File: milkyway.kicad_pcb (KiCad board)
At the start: 2 copper layers, 314.4 x 98.8 mm, 82 parts, among them J10 Conn_01x01, J11 Conn_01x01, J12 Conn_01x01, J13 Conn_01x01, J14 Conn_01x01, J15 Conn_01x01, J16 Conn_01x01, J17 Conn_01x01, J2 Conn_01x01, J3 Conn_01x01, J4 Conn_01x01, J5 Conn_01x01, J6 Conn_01x01, J7 Conn_01x01, J8 Conn_01x01, J9 Conn_01x01, SW1 SW_PUSH, SW10 SW_PUSH, SW11 SW_PUSH, SW12 SW_PUSH, SW13 SW_PUSH, SW14 SW_PUSH, SW15 SW_PUSH, SW16 SW_PUSH, SW17 KEY_SWITCH, SW17 SW_PUSH, SW18 SW_PUSH, SW19 SW_PUSH, SW2 KEY_SWITCH, SW2 SW_PUSH, SW22 SW_PUSH, SW23 SW_PUSH, SW24 SW_PUSH, SW27 SW_PUSH, SW28 SW_PUSH, SW29 SW_PUSH, SW3 SW_PUSH, SW32 SW_PUSH, SW33 SW_PUSH, SW34 SW_PUSH, SW37 SW_PUSH, SW38 SW_PUSH, SW39 SW_PUSH, SW4 KEY_SWITCH, SW4 SW_PUSH, SW42 SW_PUSH, SW43 SW_PUSH, SW44 SW_PUSH, SW47 SW_PUSH, SW48 SW_PUSH, SW49 SW_PUSH, SW5 SW_PUSH, SW52 SW_PUSH, SW53 SW_PUSH, SW54 SW_PUSH, SW57 SW_PUSH, SW58 SW_PUSH, SW6 SW_PUSH, SW60 SW_PUSH, SW61 SW_PUSH, SW62 SW_PUSH, SW67 SW_PUSH, SW7 SW_PUSH, SW72 SW_PUSH, SW8 SW_PUSH, SW9 SW_PUSH

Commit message: complete plate
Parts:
- removed SW15, SW16, SW72: SW_PUSH, kbd_SW_Hole:SW_Hole_1u
- removed the SW2 at (171.4, 104.8)
- removed the SW2 at (261.9, 104.8)
- removed the SW2 at (309.6, 104.8)
- removed the SW2 at (33.3, 104.8)
- removed the SW2 at (81.0, 104.8)
- removed SW62: SW_PUSH, kbd_SW_Hole:SW_Hole_1.75u
- removed the SW9 at (57.1, 104.8)
- removed the SW9 at (285.8, 104.8)
- added SW2: KEY_SWITCH, milkyway:SW_Hole_Split_Bksp, F.Cu at (304.8, 28.6)
- added SW2: KEY_SWITCH, milkyway:SW_Hole_Split_Rshift, F.Cu at (297.7, 85.7)
- added SW2: KEY_SWITCH, milkyway:SW_Hole_R5_all, F.Cu at (171.4, 104.8)
- turned SW4 to 0 degrees (x2)

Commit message: complete pcb
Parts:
- removed J2, J3, J4, J5, J6, J7: Conn_01x01, kbd_Hole:m2_Screw_Hole_EdgeCuts
- removed SW1, SW10, SW11, SW12 (x2), SW13 (x2), SW14 (x2), SW17, SW18 (x2), SW19, SW2, SW22, SW23, SW24, SW27, SW28, SW29, SW3, SW32, SW33, SW34, SW37, SW38, SW39, SW4, SW42, SW43, SW44, SW47, SW48, SW49, SW5, SW52, SW53, SW54, SW57, SW58, SW6, SW60 (x2), SW61, SW67, SW7, SW8 (x2), SW9 (x2): SW_PUSH, kbd_SW_Hole:SW_Hole_1u
- removed SW17, SW2: KEY_SWITCH, kbd_SW_Hole:SW_Hole_1.5u
- removed SW2: KEY_SWITCH, milkyway:SW_Hole_Split_Bksp
- removed SW2: KEY_SWITCH, milkyway:SW_Hole_Split_Rshift
- removed SW2: KEY_SWITCH, milkyway:SW_Hole_R5_all
- removed SW3: SW_PUSH, kbd_SW_Hole:SW_Hole_1.75u
- removed SW4 (x2): KEY_SWITCH, kbd_SW_Hole:SW_Hole_2.25u
- added DC00: D, kbd_Parts:Diode_TH_SMD, F.Cu at (57.1, 33.3)
- added DC01: D, kbd_Parts:Diode_TH_SMD, F.Cu at (95.2, 33.3)
- added DC02: D, kbd_Parts:Diode_TH_SMD, F.Cu at (133.3, 33.3)
- added DC03: D, kbd_Parts:Diode_TH_SMD, F.Cu at (171.4, 33.3)
- added DC04: D, kbd_Parts:Diode_TH_SMD, F.Cu at (209.6, 33.3)
- added DC05: D, kbd_Parts:Diode_TH_SMD, F.Cu at (246.4, 30.5)
- added DC06: D, kbd_Parts:Diode_TH_SMD, F.Cu at (284.5, 31.1)
- added DC07: D, kbd_Parts:Diode_TH_SMD, F.Cu at (321.5, 42.9)
- added DC10: D, kbd_Parts:Diode_TH_SMD, F.Cu at (66.7, 52.4)
- added DC11: D, kbd_Parts:Diode_TH_SMD, F.Cu at (104.8, 52.4)
- added DC12: D, kbd_Parts:Diode_TH_SMD, F.Cu at (142.9, 52.4)
- added DC13: D, kbd_Parts:Diode_TH_SMD, F.Cu at (181.0, 52.4)
- added DC14: D, kbd_Parts:Diode_TH_SMD, F.Cu at (219.1, 52.4)
- added DC15: D, kbd_Parts:Diode_TH_SMD, F.Cu at (257.2, 52.4)
- added DC16: D, kbd_Parts:Diode_TH_SMD, F.Cu at (295.3, 52.4)
- added DC20: D, kbd_Parts:Diode_TH_SMD, F.Cu at (71.4, 71.4)
- added DC21: D, kbd_Parts:Diode_TH_SMD, F.Cu at (109.5, 71.4)
- added DC22: D, kbd_Parts:Diode_TH_SMD, F.Cu at (147.6, 71.4)
- added DC23: D, kbd_Parts:Diode_TH_SMD, F.Cu at (185.7, 71.4)
- added DC24: D, kbd_Parts:Diode_TH_SMD, F.Cu at (223.8, 71.4)
- added DC25: D, kbd_Parts:Diode_TH_SMD, F.Cu at (261.9, 71.4)
- added DC26: D, kbd_Parts:Diode_TH_SMD, F.Cu at (283.4, 71.4)
- added DC30: D, kbd_Parts:Diode_TH_SMD, F.Cu at (81.0, 90.5)
- added DC31: D, kbd_Parts:Diode_TH_SMD, F.Cu at (118.1, 90.5)
- added DC32: D, kbd_Parts:Diode_TH_SMD, F.Cu at (157.2, 90.5)
- added DC33: D, kbd_Parts:Diode_TH_SMD, F.Cu at (194.3, 88.4)
- added DC34: D, kbd_Parts:Diode_TH_SMD, F.Cu at (233.4, 90.5)
- added DC35: D, kbd_Parts:Diode_TH_SMD, F.Cu at (271.5, 90.5)
- added DC36: D, kbd_Parts:Diode_TH_SMD, F.Cu at (317.5, 95.2)
- added DC40: D, kbd_Parts:Diode_TH_SMD, F.Cu at (72.4, 109.6)
- added DC41: D, kbd_Parts:Diode_TH_SMD, F.Cu at (131.0, 95.2)
- added DC42: D, kbd_Parts:Diode_TH_SMD, F.Cu at (207.2, 100.0)
- added DC45: D, kbd_Parts:Diode_TH_SMD, F.Cu at (271.5, 109.5)
- added DC46: D, kbd_Parts:Diode_TH_SMD, F.Cu at (297.7, 109.5)
- added DR00: D, kbd_Parts:Diode_TH_SMD, F.Cu at (38.1, 33.3)
- added DR01: D, kbd_Parts:Diode_TH_SMD, F.Cu at (76.2, 33.3)
- added DR02: D, kbd_Parts:Diode_TH_SMD, F.Cu at (114.3, 33.3)
- added DR03: D, kbd_Parts:Diode_TH_SMD, F.Cu at (152.4, 33.3)
- added DR04: D, kbd_Parts:Diode_TH_SMD, F.Cu at (190.5, 32.7)
- added DR05: D, kbd_Parts:Diode_TH_SMD, F.Cu at (228.6, 33.3)
- added DR06: D, kbd_Parts:Diode_TH_SMD, F.Cu at (265.4, 31.1)
- added DR07: D, kbd_Parts:Diode_TH_SMD, F.Cu at (304.8, 38.1)
- added DR10: D, kbd_Parts:Diode_TH_SMD, F.Cu at (42.9, 52.4)
- added DR11: D, kbd_Parts:Diode_TH_SMD, F.Cu at (85.7, 52.4)
- added DR12: D, kbd_Parts:Diode_TH_SMD, F.Cu at (123.8, 52.4)
- added DR13: D, kbd_Parts:Diode_TH_SMD, F.Cu at (161.9, 52.4)
- added DR14: D, kbd_Parts:Diode_TH_SMD, F.Cu at (200.0, 52.4)
- added DR15: D, kbd_Parts:Diode_TH_SMD, F.Cu at (238.1, 52.4)
- added DR16: D, kbd_Parts:Diode_TH_SMD, F.Cu at (276.2, 52.4)
- added DR17: D, kbd_Parts:Diode_TH_SMD, F.Cu at (297.7, 52.4)
- added DR20: D, kbd_Parts:Diode_TH_SMD, F.Cu at (45.2, 71.4)
- added DR21: D, kbd_Parts:Diode_TH_SMD, F.Cu at (90.5, 71.4)
- added DR22: D, kbd_Parts:Diode_TH_SMD, F.Cu at (128.6, 71.4)
- added DR23: D, kbd_Parts:Diode_TH_SMD, F.Cu at (166.7, 71.4)
- added DR24: D, kbd_Parts:Diode_TH_SMD, F.Cu at (204.8, 71.4)
- added DR25: D, kbd_Parts:Diode_TH_SMD, F.Cu at (242.9, 71.4)
- added DR26: D, kbd_Parts:Diode_TH_SMD, F.Cu at (281.0, 71.4)
- added DR30: D, kbd_Parts:Diode_TH_SMD, F.Cu at (59.5, 90.5)
- added DR31: D, kbd_Parts:Diode_TH_SMD, F.Cu at (100.0, 90.5)
- added DR32: D, kbd_Parts:Diode_TH_SMD, F.Cu at (138.1, 90.5)
- added DR33: D, kbd_Parts:Diode_TH_SMD, F.Cu at (176.2, 90.5)
- added DR34: D, kbd_Parts:Diode_TH_SMD, F.Cu at (213.4, 88.3)
- added DR35: D, kbd_Parts:Diode_TH_SMD, F.Cu at (252.4, 90.5)
- added DR36: D, kbd_Parts:Diode_TH_SMD, F.Cu at (273.8, 90.5)
- added DR40: D, kbd_Parts:Diode_TH_SMD, F.Cu at (42.9, 109.5)
- added DR41: D, kbd_Parts:Diode_TH_SMD, F.Cu at (90.5, 95.2)
- added DR42: D, kbd_Parts:Diode_TH_SMD, F.Cu at (152.4, 109.5)
- added DR43: D, kbd_Parts:Diode_TH_SMD, F.Cu at (207.2, 109.5)
- added DR46: D, kbd_Parts:Diode_TH_SMD, F.Cu at (295.3, 109.5)
- added SW0: SW_PUSH, kbd_Parts:ResetSW, F.Cu at (219.1, 37.2)
- added SWC00: SW_PUSH, kbd_SW:CherryMX_Hotswap_1u, F.Cu at (47.6, 28.6)
- added SWC01: SW_PUSH, kbd_SW:CherryMX_Hotswap_1u, F.Cu at (85.7, 28.6)
- added SWC02: SW_PUSH, kbd_SW:CherryMX_Hotswap_1u, F.Cu at (123.8, 28.6)
- added SWC03: Enc, milkyway:CherryMX_Hotswap_1u_EC12, F.Cu at (161.9, 28.6)
- added SWC04: SW_PUSH, kbd_SW:CherryMX_Hotswap_1u, F.Cu at (200.0, 28.6)
- added SWC05: SW_PUSH, kbd_SW:CherryMX_Hotswap_1u, F.Cu at (238.1, 28.6)
- added SWC06: SW_PUSH, kbd_SW:CherryMX_Hotswap_1u, F.Cu at (276.2, 28.6)
- added SWC07: SW_PUSH, kbd_SW:CherryMX_Hotswap_1u, F.Cu at (314.3, 28.6)
- added SWC10: SW_PUSH, kbd_SW:CherryMX_Hotswap_1u, F.Cu at (57.1, 47.6)
- added SWC11: SW_PUSH, kbd_SW:CherryMX_Hotswap_1u, F.Cu at (95.2, 47.6)
- added SWC12: SW_PUSH, kbd_SW:CherryMX_Hotswap_1u, F.Cu at (133.3, 47.6)
- added SWC13: SW_PUSH, kbd_SW:CherryMX_Hotswap_1u, F.Cu at (171.4, 47.6)
- added SWC14: SW_PUSH, kbd_SW:CherryMX_Hotswap_1u, F.Cu at (209.6, 47.6)
- added SWC15: SW_PUSH, kbd_SW:CherryMX_Hotswap_1u, F.Cu at (247.7, 47.6)
- added SWC16: SW_PUSH, kbd_SW:CherryMX_Hotswap_1u, F.Cu at (285.8, 47.6)
- added SWC20: SW_PUSH, kbd_SW:CherryMX_Hotswap_1u, F.Cu at (61.9, 66.7)
- added SWC21: SW_PUSH, kbd_SW:CherryMX_Hotswap_1u, F.Cu at (100.0, 66.7)
- added SWC22: SW_PUSH, kbd_SW:CherryMX_Hotswap_1u, F.Cu at (138.1, 66.7)
- added SWC23: SW_PUSH, kbd_SW:CherryMX_Hotswap_1u, F.Cu at (176.2, 66.7)
- added SWC24: SW_PUSH, kbd_SW:CherryMX_Hotswap_1u, F.Cu at (214.3, 66.7)
- added SWC25: SW_PUSH, kbd_SW:CherryMX_Hotswap_1u, F.Cu at (252.4, 66.7)
- added SWC26: SW_PUSH, kbd_SW:CherryMX_Hotswap_2.25u, F.Cu at (302.4, 66.7)
- added SWC30: SW_PUSH, kbd_SW:CherryMX_Hotswap_1u, F.Cu at (71.4, 85.7)
- added SWC31: SW_PUSH, kbd_SW:CherryMX_Hotswap_1u, F.Cu at (109.5, 85.7)
- added SWC32: SW_PUSH, kbd_SW:CherryMX_Hotswap_1u, F.Cu at (147.6, 85.7)
- added SWC33: SW_PUSH, kbd_SW:CherryMX_Hotswap_1u, F.Cu at (185.7, 85.7)
- added SWC34: SW_PUSH, kbd_SW:CherryMX_Hotswap_1u, F.Cu at (223.8, 85.7)
- added SWC35: SW_PUSH, kbd_SW:CherryMX_Hotswap_1u, F.Cu at (261.9, 85.7)
- added SWC36: SW_PUSH, kbd_SW:CherryMX_Hotswap_1u, F.Cu at (314.3, 85.7)
- added SWC401: SW_PUSH, kbd_SW:CherryMX_Hotswap_1u, F.Cu at (57.1, 104.8)
- added SWC402: SW_PUSH, kbd_SW:CherryMX_Hotswap_1.5u, F.Cu at (61.9, 104.8)
- added SWC411: SW_PUSH, milkyway:CherryMX_Solder_3u_Rev, F.Cu at (123.8, 104.8)
- added SWC412: SW_PUSH, kbd_SW:CherryMX_1u_solder, F.Cu at (104.8, 104.8)
- added SWC421: Enc, milkyway:CherryMX_Solder_1u_EC12, F.Cu at (181.0, 104.8)
- added SWC422: SW_PUSH, milkyway:CherryMX_Solder_8u7u_Rev, F.Cu at (171.4, 104.8)
- added SWC423: SW_PUSH, milkyway:CherryMX_Solder_2.75u_Rev, F.Cu at (178.6, 104.8)
- added SWC451: SW_PUSH, kbd_SW:CherryMX_Hotswap_1.5u, F.Cu at (261.9, 104.8)
- added SWC452: SW_PUSH, kbd_SW:CherryMX_Hotswap_1.5u, F.Cu at (252.4, 104.8)
- added SWC46: SW_PUSH, kbd_SW:CherryMX_Hotswap_1.5u, F.Cu at (309.6, 104.8)
- added SWR00: SW_PUSH, kbd_SW:CherryMX_Hotswap_1u, F.Cu at (28.6, 28.6)
- added SWR01: SW_PUSH, kbd_SW:CherryMX_Hotswap_1u, F.Cu at (66.7, 28.6)
- added SWR02: SW_PUSH, kbd_SW:CherryMX_Hotswap_1u, F.Cu at (104.8, 28.6)
- added SWR03: Enc, milkyway:CherryMX_Hotswap_1u_EC12, F.Cu at (142.9, 28.6)
- added SWR04: SW_PUSH, kbd_SW:CherryMX_Hotswap_1u, F.Cu at (181.0, 28.6)
- added SWR05: SW_PUSH, kbd_SW:CherryMX_Hotswap_1u, F.Cu at (219.1, 28.6)
- added SWR06: SW_PUSH, kbd_SW:CherryMX_Hotswap_1u, F.Cu at (257.2, 28.6)
- added SWR071: SW_PUSH, kbd_SW:CherryMX_Hotswap_2u, F.Cu at (304.8, 28.6)
- added SWR072: SW_PUSH, kbd_SW:CherryMX_Hotswap_1u, F.Cu at (295.3, 28.6)
- added SWR10: SW_PUSH, kbd_SW:CherryMX_Hotswap_1.5u, F.Cu at (33.3, 47.6)
- added SWR11: SW_PUSH, kbd_SW:CherryMX_Hotswap_1u, F.Cu at (76.2, 47.6)
- added SWR12: SW_PUSH, kbd_SW:CherryMX_Hotswap_1u, F.Cu at (114.3, 47.6)
- added SWR13: Enc, milkyway:CherryMX_Hotswap_1u_EC12, F.Cu at (152.4, 47.6)
- added SWR14: SW_PUSH, kbd_SW:CherryMX_Hotswap_1u, F.Cu at (190.5, 47.6)
- added SWR15: SW_PUSH, kbd_SW:CherryMX_Hotswap_1u, F.Cu at (228.6, 47.6)
- added SWR16: SW_PUSH, kbd_SW:CherryMX_Hotswap_1u, F.Cu at (266.7, 47.6)
- added SWR17: SW_PUSH, kbd_SW:CherryMX_Hotswap_1.5u, F.Cu at (307.2, 47.6)
- added SWR201: SW_PUSH, kbd_SW:CherryMX_Hotswap_1.75u, F.Cu at (35.7, 66.7)
- added SWR202: SW_PUSH, kbd_SW:CherryMX_Hotswap_1u, F.Cu at (28.6, 66.7)
- added SWR21: SW_PUSH, kbd_SW:CherryMX_Hotswap_1u, F.Cu at (81.0, 66.7)
- added SWR22: SW_PUSH, kbd_SW:CherryMX_Hotswap_1u, F.Cu at (119.1, 66.7)
- added SWR23: Enc, milkyway:CherryMX_Hotswap_1u_EC12, F.Cu at (157.2, 66.7)
- added SWR24: SW_PUSH, kbd_SW:CherryMX_Hotswap_1u, F.Cu at (195.3, 66.7)
- added SWR25: SW_PUSH, kbd_SW:CherryMX_Hotswap_1u, F.Cu at (233.4, 66.7)
- added SWR26: SW_PUSH, kbd_SW:CherryMX_Hotswap_1u, F.Cu at (271.5, 66.7)
- added SWR30: SW_PUSH, kbd_SW:CherryMX_Hotswap_2.75u, F.Cu at (40.5, 85.7)
- added SWR31: SW_PUSH, kbd_SW:CherryMX_Hotswap_1u, F.Cu at (90.5, 85.7)
- added SWR32: SW_PUSH, kbd_SW:CherryMX_Hotswap_1u, F.Cu at (128.6, 85.7)
- added SWR33: Enc, milkyway:CherryMX_Hotswap_1u_EC12, F.Cu at (166.7, 85.7)
- added SWR34: SW_PUSH, kbd_SW:CherryMX_Hotswap_1u, F.Cu at (204.8, 85.7)
- added SWR35: SW_PUSH, kbd_SW:CherryMX_Hotswap_1u, F.Cu at (242.9, 85.7)
- added SWR361: SW_PUSH, kbd_SW:CherryMX_Hotswap_2.75u, F.Cu at (297.7, 85.7)
- added SWR362: SW_PUSH, kbd_SW:CherryMX_Hotswap_1.75u, F.Cu at (288.1, 85.7)
- added SWR40: SW_PUSH, kbd_SW:CherryMX_Hotswap_1.5u, F.Cu at (33.3, 104.8)
- added SWR411: SW_PUSH, kbd_SW:CherryMX_Hotswap_1.5u, F.Cu at (81.0, 104.8)
- added SWR412: SW_PUSH, kbd_SW:CherryMX_Hotswap_1.5u, F.Cu at (90.5, 104.8)
- added SWR421: Enc, milkyway:CherryMX_Solder_1u_EC12, F.Cu at (161.9, 104.8)
- added SWR422: SW_PUSH, milkyway:CherryMX_Solder_2u_Rev, F.Cu at (133.3, 104.8)
- added SWR431: SW_PUSH, milkyway:CherryMX_Solder_3u_Rev, F.Cu at (219.1, 104.8)
- added SWR432: SW_PUSH, milkyway:CherryMX_Solder_2.25u_Rev, F.Cu at (226.2, 104.8)
- added SWR461: SW_PUSH, kbd_SW:CherryMX_Hotswap_1u, F.Cu at (285.8, 104.8)
- added SWR462: SW_PUSH, kbd_SW:CherryMX_Hotswap_1.5u, F.Cu at (281.0, 104.8)
- added U1: Raspberry_Pi_Pico, milkyway:Raspberry_Pi_Pico, F.Cu at (261.9, 28.6)
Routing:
- net Col0: track 0.00 -> 505.5 mm, vias 0 -> 1
- net Col1: track 0.00 -> 443.4 mm, vias 0 -> 6
- net Row3: track 0.00 -> 435.4 mm, vias 0 -> 3
- net Col2: track 0.00 -> 429.7 mm, vias 0 -> 8
- net Row4: track 0.00 -> 417.8 mm, vias 0 -> 1
- net Row0: track 0.00 -> 404.9 mm
- net Row1: track 0.00 -> 379.8 mm
- net GND: track 0.00 -> 377.6 mm, vias 0 -> 4
- net Row2: track 0.00 -> 373.8 mm
- net Col3: track 0.00 -> 349.9 mm, vias 0 -> 8
- net Col6: track 0.00 -> 284.5 mm, vias 0 -> 6
- net Col5: track 0.00 -> 256.1 mm, vias 0 -> 6
- net Col4: track 0.00 -> 254.4 mm, vias 0 -> 5
- net Rot5B: track 0.00 -> 192.9 mm, vias 0 -> 4
- net Rot5A: track 0.00 -> 181.6 mm, vias 0 -> 4
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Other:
- board size 314.4 x 98.8 mm -> 304.4 x 98.8 mm

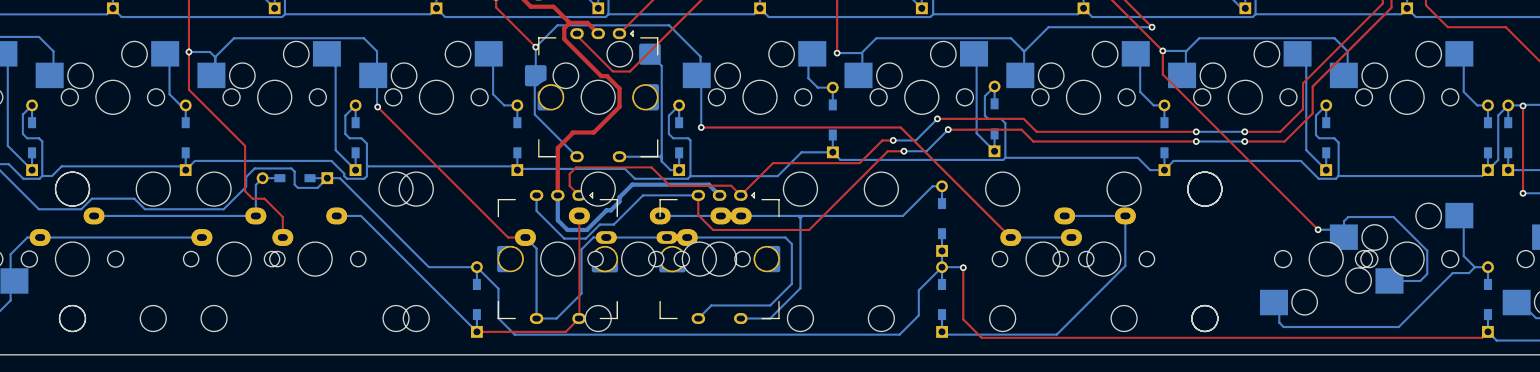
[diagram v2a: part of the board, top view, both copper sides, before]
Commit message: スタビバー上を通る配線を修正
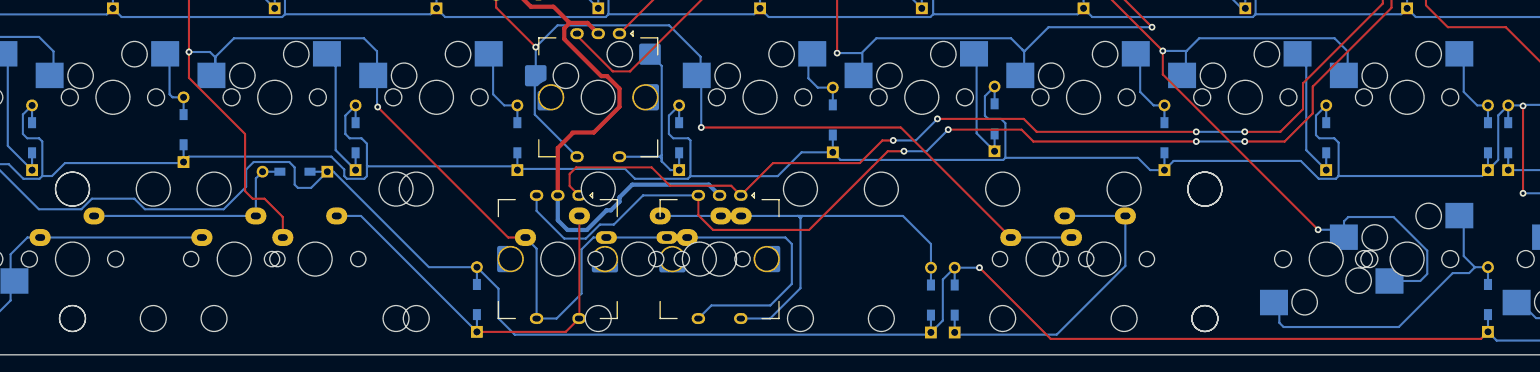
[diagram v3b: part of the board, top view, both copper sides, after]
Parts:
- moved DC42 9.68 mm to (205.9, 109.6)
- moved DR43 1.49 mm to (208.7, 109.6)
- moved DC31 0.99 mm to (117.9, 89.5)
- moved DC41 0.76 mm to (131.0, 94.5)
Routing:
- net Row4: track 417.8 -> 415.5 mm
- net Net-(DR43-Pad1): track 40.1 -> 38.6 mm
- net Net-(DC42-Pad2): track 54.8 -> 56.2 mm
- net Net-(DC41-Pad2): track 25.9 -> 26.6 mm
- net Net-(DC31-Pad2): track 9.65 -> 9.00 mm

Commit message: footprint miss thx salicylic acid san
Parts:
- SWR30: footprint kbd_SW:CherryMX_Hotswap_2.75u -> kbd_SW:CherryMX_Hotswap_2.25u
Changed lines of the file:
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@@
       (net 32 "Net-(DC34-Pad2)") (pinfunction "2") (pintype "passive"))
   )
-  (footprint "kbd_SW:CherryMX_Hotswap_2.75u" (layer "F.Cu")
+  (footprint "kbd_SW:CherryMX_Hotswap_2.25u" (layer "F.Cu")
     (at 40.48125 85.725)
     (property "Sheetfile" "milkyway.kicad_sch")
     (property "Sheetname" "")
     (attr smd)
-    (fp_text reference "SWR30" (at 7.402499 8.08) (layer "F.SilkS") hide
-      (effects (font (size 1 1) (thickness 0.15)))
+    (fp_text reference "SWR30" (at 0 4.7625) (layer "B.SilkS")
+      (effects (font (size 1 1) (thickness 0.15)) (justify mirror))
     )
     (fp_text value "SW_PUSH" (at -6.997501 -8.12) (layer "F.Fab") hide
       (effects (font (size 1 1) (thickness 0.15)))
     )
+    (fp_line (start -6.08 -0.876) (end -2.47 -0.876) (layer "B.SilkS") (width 0.15))
+    (fp_line (start 4.82 -2.876) (end 4.82 -6.784) (layer "B.SilkS") (width 0.15))
+    (fp_line (start 4.82 -6.784) (end -3.805 -6.784) (layer "B.SilkS") (width 0.15))
     (fp_line (start 4.82 -2.83) (end -0.23 -2.784) (layer "B.SilkS") (width 0.15))
-    (fp_line (start -6.08 -0.876) (end -2.47 -0.876) (layer "B.SilkS") (width 0.15))
-    (fp_line (start 4.82 -6.784) (end -3.805 -6.784) (layer "B.SilkS") (width 0.15))
-    (fp_line (start 4.82 -2.876) (end 4.82 -6.784) (layer "B.SilkS") (width 0.15))
     (fp_line (start -6.08 -4.83) (end -6.08 -0.885) (layer "B.SilkS") (width 0.15))
+    (fp_arc (start -2.465 -0.9) (mid -1.724361 -2.308061) (end -0.205 -2.78) (layer "B.SilkS") (width 0.15))
     (fp_arc (start -6.069 -4.9) (mid -5.327189 -6.31089) (end -3.805 -6.784) (layer "B.SilkS") (width 0.15))
-    (fp_arc (start -2.465 -0.9) (mid -1.724361 -2.308061) (end -0.205 -2.78) (layer "B.SilkS") (width 0.15))
     (fp_poly (pts
         (xy -6.08 -0.86)
@@
         (xy -6.09 -4.22)
       ) (layer "B.SilkS") (width 0.15) (fill solid))
-    (fp_line (start 26.19 -9.525) (end -26.19 -9.525) (layer "F.Fab") (width 0.15))
+    (fp_line (start 6 -7) (end 7 -7) (layer "F.Fab") (width 0.15))
+    (fp_line (start 21.43125 -9.525) (end -21.43125 -9.525) (layer "F.Fab") (width 0.15))
+    (fp_line (start -7 7) (end -7 6) (layer "F.Fab") (width 0.15))
+    (fp_line (start -7 -6) (end -7 -7) (layer "F.Fab") (width 0.15))
+    (fp_line (start 7 -7) (end 7 -6) (layer "F.Fab") (width 0.15))
+    (fp_line (start -21.43125 -9.525) (end -21.43125 9.525) (layer "F.Fab") (width 0.15))
+    (fp_line (start -7 -7) (end -6 -7) (layer "F.Fab") (width 0.15))
+    (fp_line (start 21.43125 9.525) (end 21.43125 -9.525) (layer "F.Fab") (width 0.15))
+    (fp_line (start -21.43125 9.525) (end 21.43125 9.525) (layer "F.Fab") (width 0.15))
+    (fp_line (start 7 6) (end 7 7) (layer "F.Fab") (width 0.15))
     (fp_line (start 7 7) (end 6 7) (layer "F.Fab") (width 0.15))
     (fp_line (start -6 7) (end -7 7) (layer "F.Fab") (width 0.15))
-    (fp_line (start 26.19 9.525) (end 26.19 -9.525) (layer "F.Fab") (width 0.15))
-    (fp_line (start -26.19 -9.525) (end -26.19 9.525) (layer "F.Fab") (width 0.15))
-    (fp_line (start 7 6) (end 7 7) (layer "F.Fab") (width 0.15))
-    (fp_line (start -7 -6) (end -7 -7) (layer "F.Fab") (width 0.15))
-    (fp_line (start 7 -7) (end 7 -6) (layer "F.Fab") (width 0.15))
-    (fp_line (start 6 -7) (end 7 -7) (layer "F.Fab") (width 0.15))
-    (fp_line (start -26.19 9.525) (end 26.19 9.525) (layer "F.Fab") (width 0.15))
-    (fp_line (start -7 -7) (end -6 -7) (layer "F.Fab") (width 0.15))
-    (fp_line (start -7 7) (end -7 6) (layer "F.Fab") (width 0.15))
     (pad "" np_thru_hole circle locked (at 11.9 -7 180) (size 3.05 3.05) (drill 3.05) (layers *.Cu *.Mask))
+    (pad "" np_thru_hole circle locked (at -3.81 -2.54 180) (size 3 3) (drill 3) (layers *.Cu *.Mask))
+    (pad "" np_thru_hole circle locked (at -5.08 0) (size 1.8 1.8) (drill 1.8) (layers *.Cu *.Mask))
     (pad "" np_thru_hole circle locked (at 5.08 0) (size 1.8 1.8) (drill 1.8) (layers *.Cu *.Mask))
     (pad "" np_thru_hole circle locked (at -11.9 -7 180) (size 3.05 3.05) (drill 3.05) (layers *.Cu *.Mask))
+    (pad "" np_thru_hole circle locked (at 11.9 8.24 180) (size 4 4) (drill 4) (layers *.Cu *.Mask))
     (pad "" np_thru_hole circle locked (at 0 0 90) (size 4 4) (drill 4) (layers *.Cu *.Mask))
-    (pad "" np_thru_hole circle locked (at 11.9 8.24 180) (size 4 4) (drill 4) (layers *.Cu *.Mask))
+    (pad "" np_thru_hole circle locked (at 2.54 -5.08 180) (size 3 3) (drill 3) (layers *.Cu *.Mask))
     (pad "" np_thru_hole circle locked (at -11.9 8.24 180) (size 4 4) (drill 4) (layers *.Cu *.Mask))
-    (pad "" np_thru_hole circle locked (at -3.81 -2.54 180) (size 3 3) (drill 3) (layers *.Cu *.Mask))
-    (pad "" np_thru_hole circle locked (at -5.08 0) (size 1.8 1.8) (drill 1.8) (layers *.Cu *.Mask))
-    (pad "" np_thru_hole circle locked (at 2.54 -5.08 180) (size 3 3) (drill 3) (layers *.Cu *.Mask))
     (pad "1" smd rect locked (at -6.9 -2.54 180) (size 3.3 3) (drill (offset 0.5 0)) (layers "B.Cu" "B.Paste" "B.Mask")
       (net 77 "Col0") (pinfunction "1") (pintype "passive"))

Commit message: pipicoフットプリント修正 配線かっこよく
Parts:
- moved DR41 0.38 mm to (90.5, 95.6)
- moved U1 0.06 mm to (262.0, 28.6)
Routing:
- net Row3: track 435.7 -> 441.7 mm
- net Col3: track 349.9 -> 355.0 mm, vias 8 -> 7
- net Rot3A: track 137.9 -> 141.3 mm
- net Row4: track 415.5 -> 418.4 mm
- net Rot2A: track 124.1 -> 126.3 mm
- net Col2: track 429.7 -> 428.3 mm
- net Col5: track 256.1 -> 257.4 mm
- net Col0: track 505.5 -> 504.7 mm
- net Row0: track 404.9 -> 405.6 mm
- net Rot4A: track 146.0 -> 146.6 mm
- net Rot5B: track 192.9 -> 192.4 mm
